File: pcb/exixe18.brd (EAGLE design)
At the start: 20 x 40 mm, 50 parts

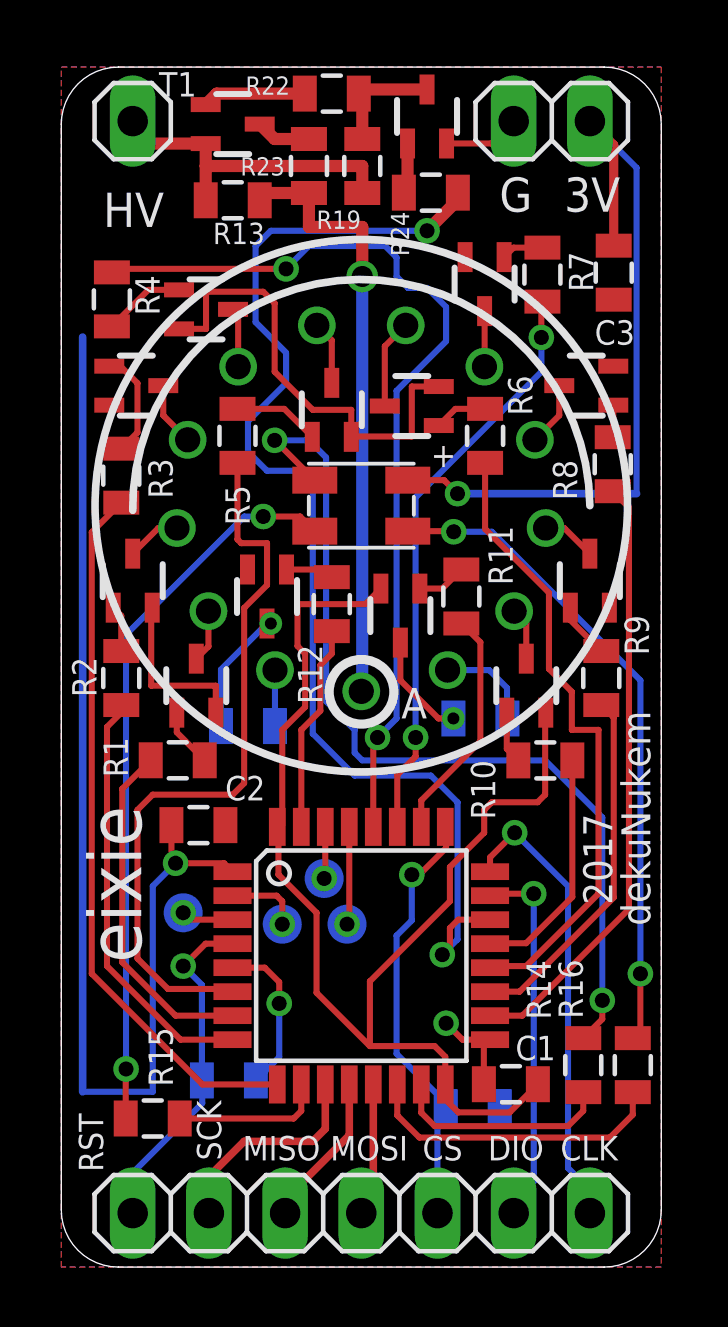
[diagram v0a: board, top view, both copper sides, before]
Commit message: added pulldown on boot0
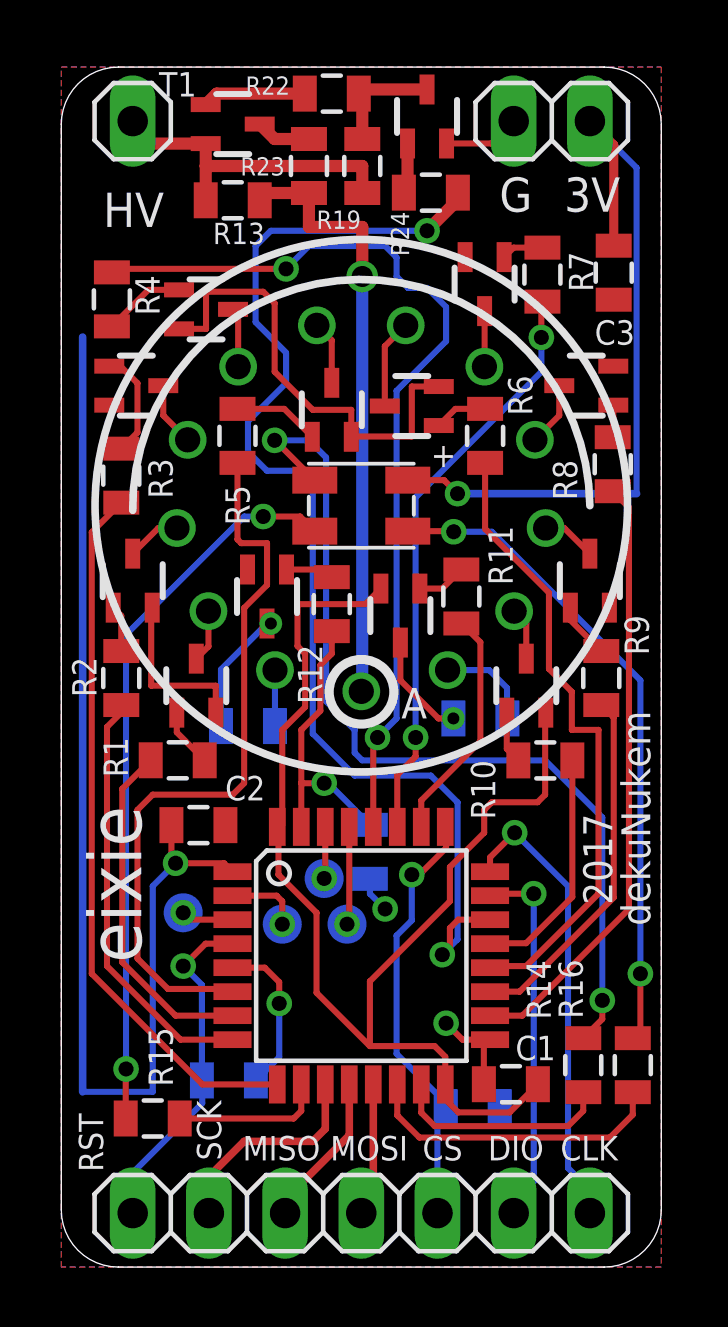
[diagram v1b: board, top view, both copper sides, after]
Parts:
- added R25: 68K, joyAnalog:0805
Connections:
- net GND: now also R25.1
- net STM_DOT_RIGHT: now also R25.2
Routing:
- net STM_DOT_RIGHT: track 6.95 -> 9.81 mm, vias 0 -> 1
- net GND: track 65.4 -> 66.6 mm, vias 0 -> 1
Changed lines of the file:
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@@
 <grid distance="5" unitdist="mil" unit="mil" style="lines" multiple="1" display="no" altdistance="1" altunitdist="mil" altunit="mil"/>
 <layers>
-<layer number="1" name="Top" color="4" fill="1" visible="yes" active="yes"/>
+<layer number="1" name="Top" color="4" fill="1" visible="no" active="yes"/>
 <layer number="2" name="Route2" color="1" fill="3" visible="no" active="yes"/>
 <layer number="3" name="Route3" color="4" fill="3" visible="no" active="yes"/>
@@
 <attribute name="NAME" x="5.461" y="17.2085" size="0.8128" layer="26" rot="MR180"/>
 </element>
+<element name="R25" library="joyAnalog" package="0805" value="68K" x="10.287" y="13.843" smashed="yes" rot="MR90">
+<attribute name="NAME" x="11.3665" y="13.843" size="0.8128" layer="26" rot="MR90"/>
+</element>
 </elements>
 <signals>
@@
 <wire x1="12.842" y1="37.454" x2="14.334" y2="37.454" width="0.2032" layer="1"/>
 <wire x1="14.334" y1="37.454" x2="15.08" y2="38.2" width="0.2032" layer="1"/>
+<contactref element="R25" pad="1"/>
+<via x="10.795" y="11.938" extent="1-16" drill="0.5"/>
+<wire x1="10.287" y1="12.943" x2="10.287" y2="12.446" width="0.2032" layer="16"/>
+<wire x1="10.287" y1="12.446" x2="10.795" y2="11.938" width="0.2032" layer="16"/>
 </signal>
 <signal name="N$1">
@@
 <wire x1="8.636" y1="20.066" x2="8.636" y2="18.542" width="0.2032" layer="1"/>
 <wire x1="8.636" y1="18.542" x2="8.001" y2="17.907" width="0.2032" layer="1"/>
-<wire x1="8.001" y1="17.907" x2="8.001" y2="14.6746" width="0.2032" layer="1"/>
+<wire x1="8.001" y1="17.907" x2="8.001" y2="16.129" width="0.2032" layer="1"/>
+<wire x1="8.001" y1="16.129" x2="8.001" y2="14.6746" width="0.2032" layer="1"/>
 <wire x1="8.001" y1="14.6746" x2="8" y2="14.6736" width="0.2032" layer="1"/>
+<contactref element="R25" pad="2"/>
+<wire x1="8.001" y1="16.129" x2="8.763" y2="16.129" width="0.2032" layer="1"/>
+<via x="8.763" y="16.129" extent="1-16" drill="0.5"/>
+<wire x1="8.763" y1="16.129" x2="8.901" y2="16.129" width="0.2032" layer="16"/>
+<wire x1="8.901" y1="16.129" x2="10.287" y2="14.743" width="0.2032" layer="16"/>
 </signal>
 <signal name="STM_6">
